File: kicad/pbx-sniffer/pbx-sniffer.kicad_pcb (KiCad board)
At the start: 2 copper layers, 377 parts, among them J49 Conn_01x02_Socket, J50 Conn_01x02_Socket, J51 Conn_01x02_Socket, J52 Conn_01x02_Socket, J53 Conn_01x02_Socket, J54 Conn_01x02_Socket, J55 Conn_01x02_Socket, J56 Conn_01x02_Socket, J57 Conn_01x02_Socket, J58 Conn_01x02_Socket, J59 Conn_01x02_Socket, J60 Conn_01x02_Socket, J61 Conn_01x02_Socket, J62 Conn_01x02_Socket, J63 Conn_01x02_Socket, J64 Conn_01x02_Socket, K10 Relay_SPDT, K11 Relay_SPST-NO, K12 Relay_SPDT, K13 Relay_SPST-NO, K14 Relay_SPDT, K15 Relay_SPST-NO, K16 Relay_SPDT, K17 Relay_SPST-NO, K18 Relay_SPDT, K19 Relay_SPST-NO, K20 Relay_SPDT, K21 Relay_SPST-NO, K22 Relay_SPDT, K23 Relay_SPST-NO, K24 Relay_SPDT, K25 Relay_SPST-NO, K26 Relay_SPDT, K27 Relay_SPST-NO, K28 Relay_SPDT, K29 Relay_SPST-NO, K3 Relay_SPST-NO, K30 Relay_SPDT, K31 Relay_SPST-NO, K32 Relay_SPDT, K33 Relay_SPST-NO, K34 Relay_SPDT, K35 Relay_SPST-NO, K36 Relay_SPDT, K37 Relay_SPST-NO, K38 Relay_SPDT, K39 Relay_SPST-NO, K4 Relay_SPDT, K40 Relay_SPDT, K41 Relay_SPST-NO, K42 Relay_SPDT, K43 Relay_SPST-NO, K44 Relay_SPDT, K45 Relay_SPST-NO, K46 Relay_SPDT, K47 Relay_SPST-NO, K48 Relay_SPDT, K49 Relay_SPST-NO, K5 Relay_SPST-NO, K50 Relay_SPDT, K6 Relay_SPDT, K7 Relay_SPST-NO, K8 Relay_SPDT, K9 Relay_SPST-NO, Q10 PMOS, Q11 PMOS, Q12 PMOS, Q13 PMOS, Q14 PMOS, Q15 PMOS, Q16 PMOS, Q17 PMOS, Q18 PMOS, Q19 PMOS, Q20 PMOS, Q21 PMOS, Q22 PMOS, Q23 PMOS, Q24 PMOS, Q25 PMOS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

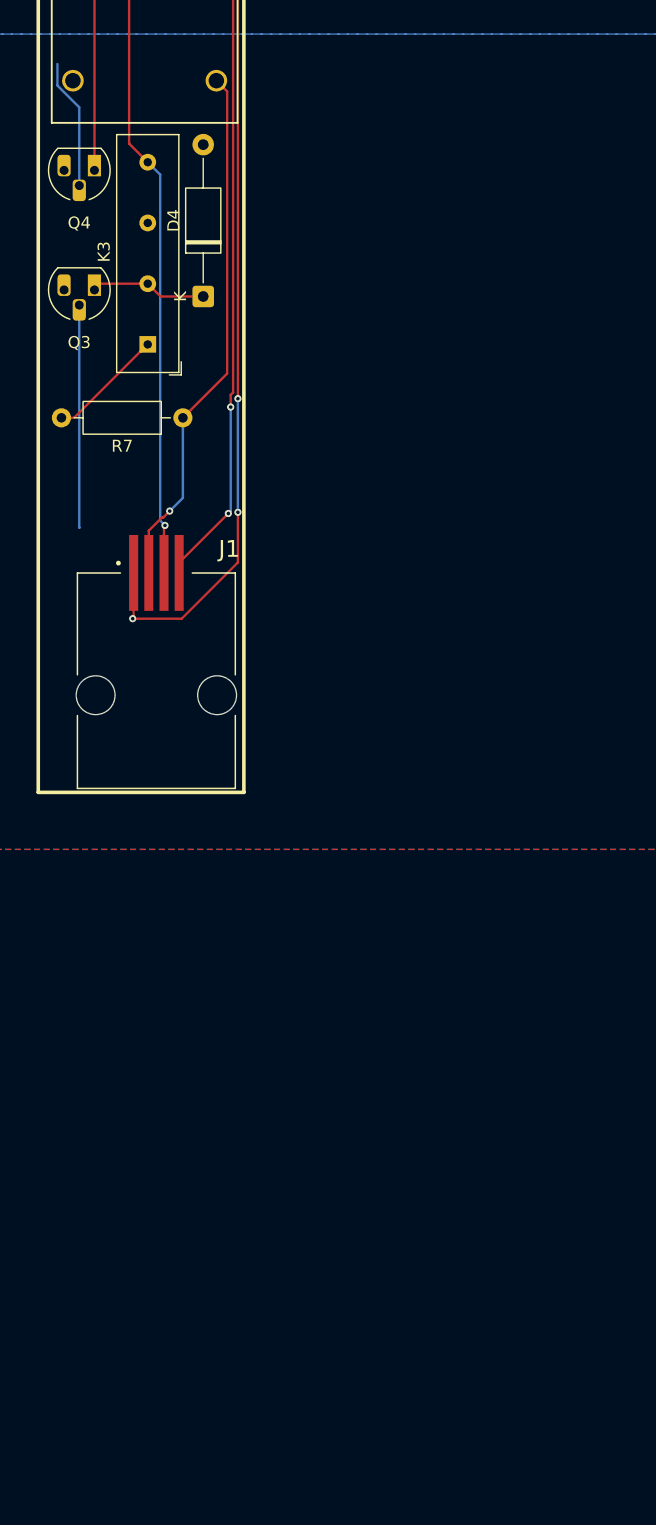
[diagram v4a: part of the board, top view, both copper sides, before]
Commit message: added solderjumpers for the control relays
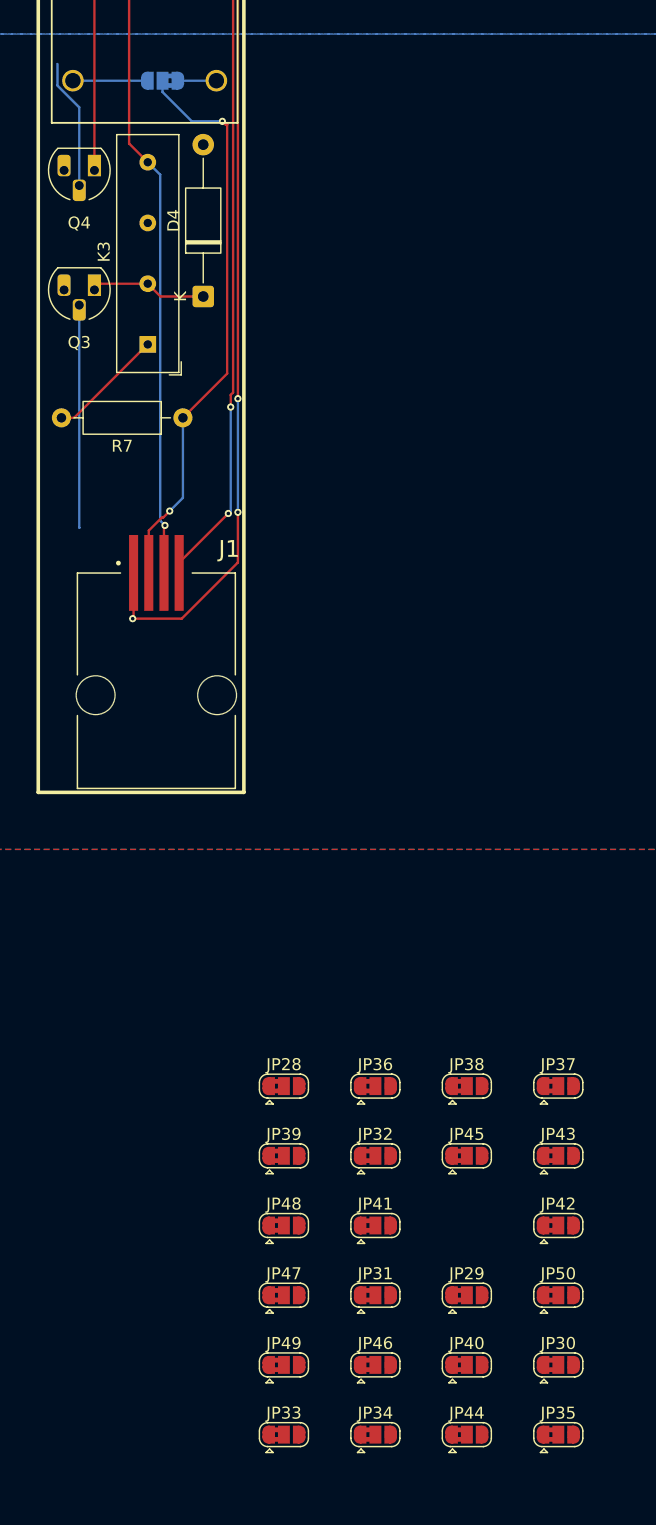
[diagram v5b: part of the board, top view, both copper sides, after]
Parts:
- added JP27: Jumper_3_Bridged12, Jumper:SolderJumper-3_P1.3mm_Bridged2Bar12_RoundedPad1.0x1.5mm, B.Cu at (142.8, 196.8)
- added JP28: Jumper_3_Bridged12, Jumper:SolderJumper-3_P1.3mm_Bridged2Bar12_RoundedPad1.0x1.5mm, F.Cu at (152.9, 280.9)
- added JP29: Jumper_3_Bridged12, Jumper:SolderJumper-3_P1.3mm_Bridged2Bar12_RoundedPad1.0x1.5mm, F.Cu at (168.2, 298.4)
- added JP30: Jumper_3_Bridged12, Jumper:SolderJumper-3_P1.3mm_Bridged2Bar12_RoundedPad1.0x1.5mm, F.Cu at (175.9, 304.2)
- added JP31: Jumper_3_Bridged12, Jumper:SolderJumper-3_P1.3mm_Bridged2Bar12_RoundedPad1.0x1.5mm, F.Cu at (160.6, 298.4)
- added JP32: Jumper_3_Bridged12, Jumper:SolderJumper-3_P1.3mm_Bridged2Bar12_RoundedPad1.0x1.5mm, F.Cu at (160.6, 286.7)
- added JP33: Jumper_3_Bridged12, Jumper:SolderJumper-3_P1.3mm_Bridged2Bar12_RoundedPad1.0x1.5mm, F.Cu at (152.9, 310.1)
- added JP34: Jumper_3_Bridged12, Jumper:SolderJumper-3_P1.3mm_Bridged2Bar12_RoundedPad1.0x1.5mm, F.Cu at (160.6, 310.1)
- added JP35: Jumper_3_Bridged12, Jumper:SolderJumper-3_P1.3mm_Bridged2Bar12_RoundedPad1.0x1.5mm, F.Cu at (175.9, 310.1)
- added JP36: Jumper_3_Bridged12, Jumper:SolderJumper-3_P1.3mm_Bridged2Bar12_RoundedPad1.0x1.5mm, F.Cu at (160.6, 280.9)
- added JP37: Jumper_3_Bridged12, Jumper:SolderJumper-3_P1.3mm_Bridged2Bar12_RoundedPad1.0x1.5mm, F.Cu at (175.9, 280.9)
- added JP38: Jumper_3_Bridged12, Jumper:SolderJumper-3_P1.3mm_Bridged2Bar12_RoundedPad1.0x1.5mm, F.Cu at (168.2, 280.9)
- added JP39: Jumper_3_Bridged12, Jumper:SolderJumper-3_P1.3mm_Bridged2Bar12_RoundedPad1.0x1.5mm, F.Cu at (152.9, 286.7)
- added JP40: Jumper_3_Bridged12, Jumper:SolderJumper-3_P1.3mm_Bridged2Bar12_RoundedPad1.0x1.5mm, F.Cu at (168.2, 304.2)
- added JP41: Jumper_3_Bridged12, Jumper:SolderJumper-3_P1.3mm_Bridged2Bar12_RoundedPad1.0x1.5mm, F.Cu at (160.6, 292.6)
- added JP42: Jumper_3_Bridged12, Jumper:SolderJumper-3_P1.3mm_Bridged2Bar12_RoundedPad1.0x1.5mm, F.Cu at (175.9, 292.6)
- added JP43: Jumper_3_Bridged12, Jumper:SolderJumper-3_P1.3mm_Bridged2Bar12_RoundedPad1.0x1.5mm, F.Cu at (175.9, 286.7)
- added JP44: Jumper_3_Bridged12, Jumper:SolderJumper-3_P1.3mm_Bridged2Bar12_RoundedPad1.0x1.5mm, F.Cu at (168.2, 310.1)
- added JP45: Jumper_3_Bridged12, Jumper:SolderJumper-3_P1.3mm_Bridged2Bar12_RoundedPad1.0x1.5mm, F.Cu at (168.2, 286.7)
- added JP46: Jumper_3_Bridged12, Jumper:SolderJumper-3_P1.3mm_Bridged2Bar12_RoundedPad1.0x1.5mm, F.Cu at (160.6, 304.2)
- added JP47: Jumper_3_Bridged12, Jumper:SolderJumper-3_P1.3mm_Bridged2Bar12_RoundedPad1.0x1.5mm, F.Cu at (152.9, 298.4)
- added JP48: Jumper_3_Bridged12, Jumper:SolderJumper-3_P1.3mm_Bridged2Bar12_RoundedPad1.0x1.5mm, F.Cu at (152.9, 292.6)
- added JP49: Jumper_3_Bridged12, Jumper:SolderJumper-3_P1.3mm_Bridged2Bar12_RoundedPad1.0x1.5mm, F.Cu at (152.9, 304.2)
- added JP50: Jumper_3_Bridged12, Jumper:SolderJumper-3_P1.3mm_Bridged2Bar12_RoundedPad1.0x1.5mm, F.Cu at (175.9, 298.4)
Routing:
- net Net-(JP27-B): track 0.00 -> 6.20 mm
- net /Input Phone Jacks/Line Control0/Tpbx: track 44.3 -> 47.9 mm, vias 1 -> 2
- net Net-(JP27-A): track 0.00 -> 3.20 mm
